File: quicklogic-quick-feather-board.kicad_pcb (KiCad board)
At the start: 6 copper layers, 50.8 x 22.9 mm, 88 parts, among them IC1 EOS-S3, J1 825437-4, J2 1x12_pinhead, J3 1x16_pinhead, J4 S2B-PH-SM4-TB_LF__SN_, J5 0473460001, J6 FTSH-105-01-L-DV-K, Q1 BSS138AKA, Q2 BSS84, Q3 RV1C002UN, Q4 RV1C002UN, Q5 RV1C002UN, U1 TPS62821DLCR, U2 MCP73831T-2ACI_OT, U3 GD25Q16CWIGR, U4 DPS310, U5 MC3635, X1 ECS-_327-12_5-34B-TR

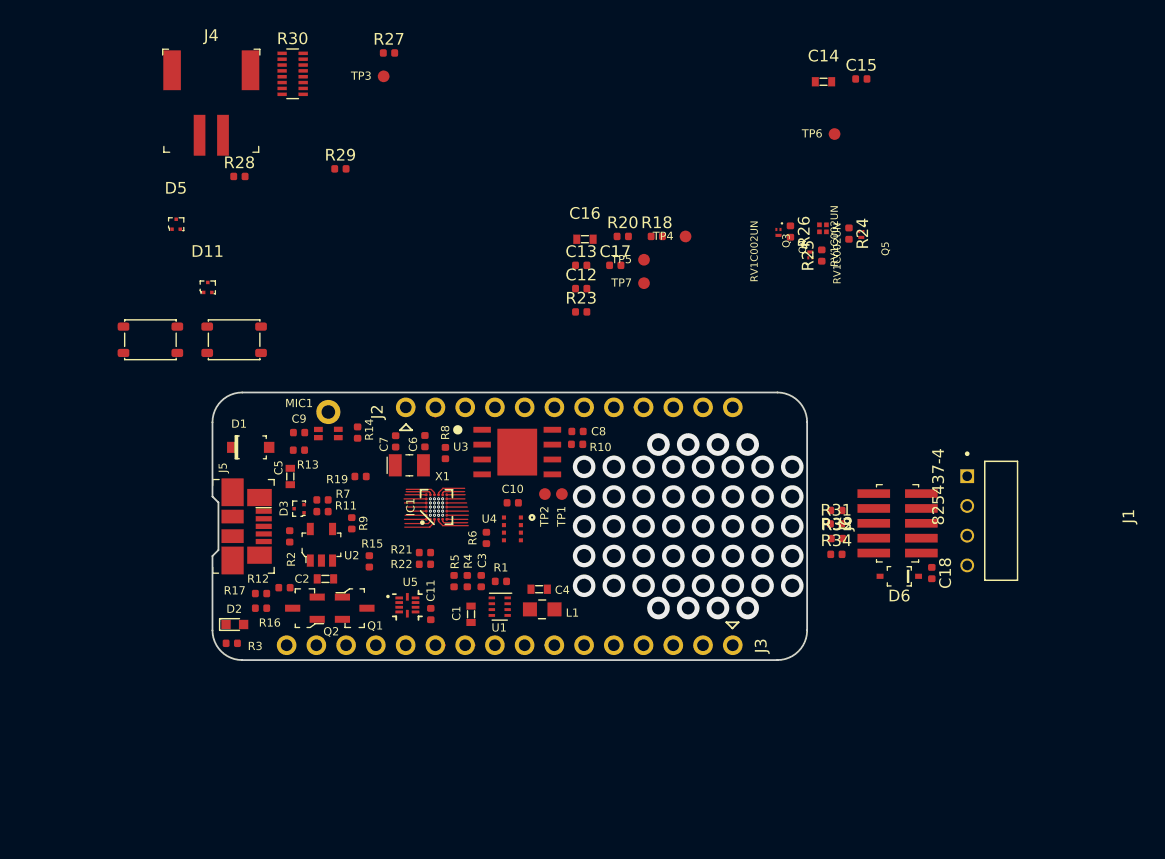
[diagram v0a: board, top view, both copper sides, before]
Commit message: Updated 3D models
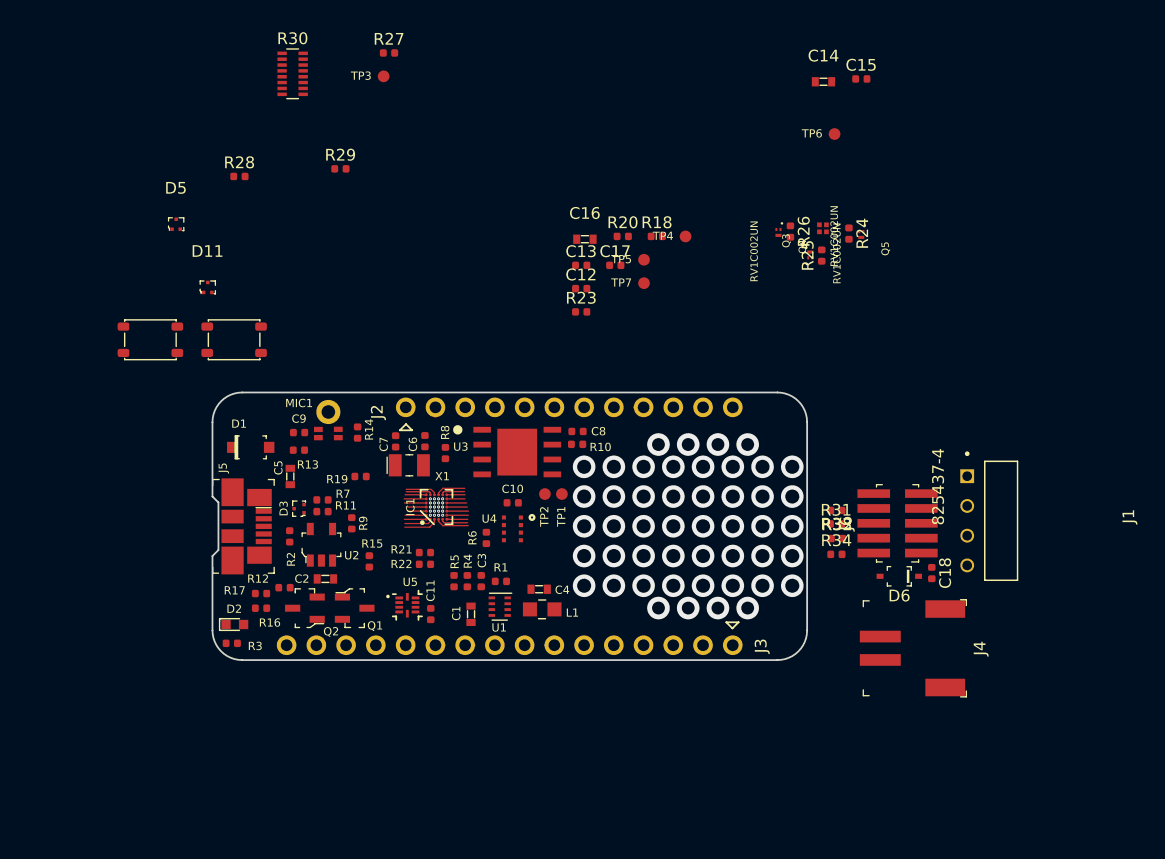
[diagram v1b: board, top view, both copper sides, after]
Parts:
- moved J4 72.0 mm to (180.2, 115.4), turned to 270 degrees

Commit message: Removed prototyping area, updated component placement
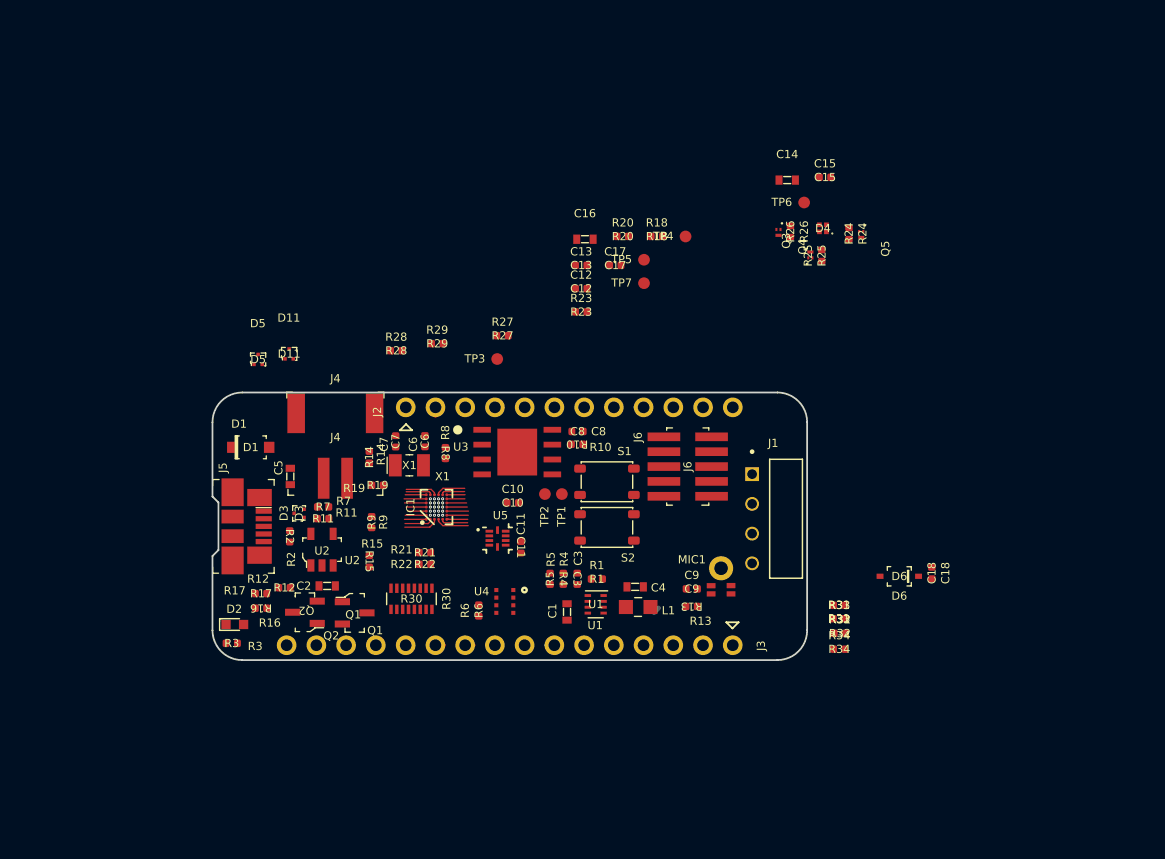
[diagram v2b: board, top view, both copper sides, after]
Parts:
- moved J4 48.8 mm to (133.6, 100.9), turned to 0 degrees
- moved R30 46.0 mm to (140.1, 111.2), turned to 270 degrees
- moved S1 40.8 mm to (156.8, 101.2), turned to 180 degrees
- moved C9 36.1 mm to (164.1, 110.3)
- moved MIC1 36.1 mm to (166.6, 108.6)
- moved R13 36.1 mm to (164.0, 111.8)
- moved S2 35.7 mm to (156.8, 105.1), turned to 180 degrees
- moved TP3 26.0 mm to (147.4, 90.8)
- moved R27 26.0 mm to (147.9, 88.7)
- moved R28 20.0 mm to (138.8, 90.0)
- moved J6 18.6 mm to (163.7, 99.9)
- moved J1 18.4 mm to (169.2, 100.5)
- moved R29 17.1 mm to (142.3, 89.4)
- moved D5 13.5 mm to (127.0, 90.8)
- moved C11 9.58 mm to (149.4, 106.8)
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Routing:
- net (no net): vias 48 -> 0
- removed copper zone on In2.Cu, net GND

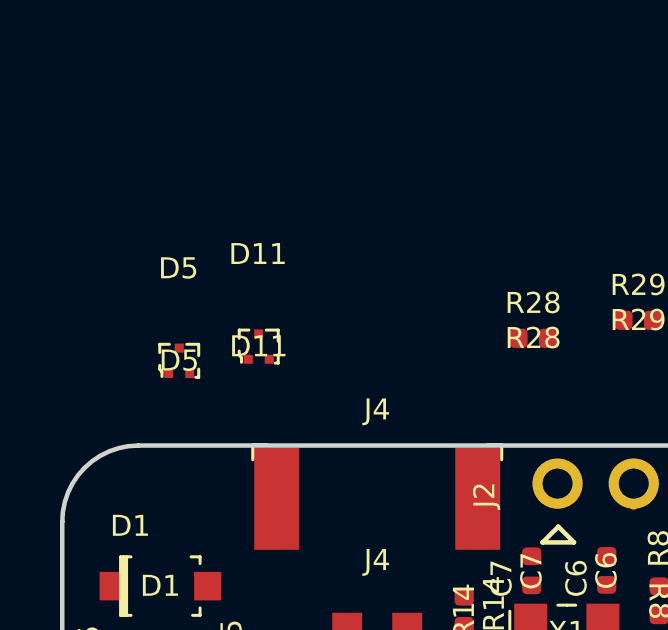
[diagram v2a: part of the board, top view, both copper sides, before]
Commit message: Changed MPN for buttons, updated 3D models
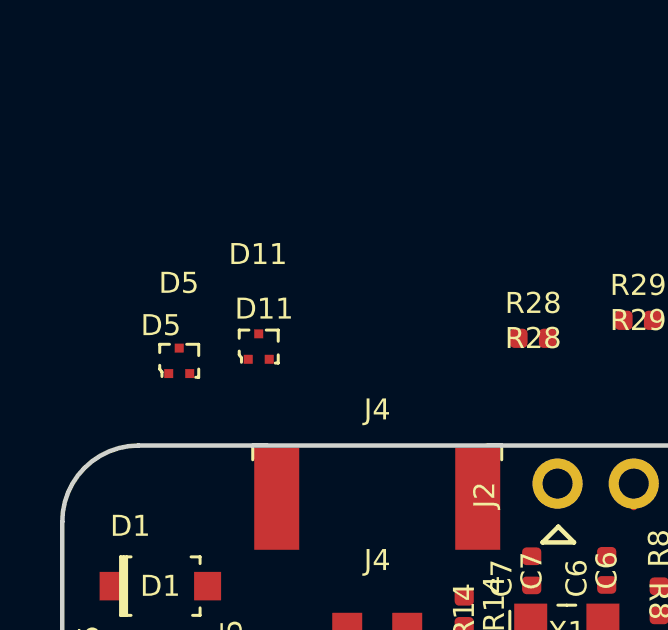
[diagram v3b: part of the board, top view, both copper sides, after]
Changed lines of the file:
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@@
-(kicad_pcb (version 20171130) (host pcbnew 5.1.4+dfsg1-1~bpo9+1)
+(kicad_pcb (version 20171130) (host pcbnew 5.1.4-e60b266~84~ubuntu18.04.1)
   (general
     (thickness 1.6)
@@
     (fp_line (start -0.525 0.225) (end -0.525 -0.425) (layer F.Fab) (width 0.1))
     (fp_line (start -0.35 0.425) (end 0.525 0.425) (layer F.Fab) (width 0.1))
-    (fp_text user %R (at 0 0) (layer F.SilkS)
+    (fp_text user %R (at 0.18 -1.255) (layer F.SilkS)
       (effects (font (size 0.7 0.7) (thickness 0.15)))
     )
@@
     (descr http://www.ti.com/lit/ds/symlink/tpd2eusb30.pdf)
     (attr smd)
-    (fp_text reference D5 (at -0.025 -3.075) (layer F.SilkS)
+    (fp_text reference D5 (at -0.01 -2.59) (layer F.SilkS)
       (effects (font (size 0.7 0.7) (thickness 0.15)))
     )
@@
     (fp_line (start -0.525 0.225) (end -0.525 -0.425) (layer F.Fab) (width 0.1))
     (fp_line (start -0.35 0.425) (end 0.525 0.425) (layer F.Fab) (width 0.1))
-    (fp_text user %R (at 0 0) (layer F.SilkS)
-      (effects (font (size 0.7 0.7) (thickness 0.15)))
-    )
+    (fp_text user %R (at -0.61 -1.18) (layer F.SilkS)
+      (effects (font (size 0.7 0.7) (thickness 0.15)))
+    )

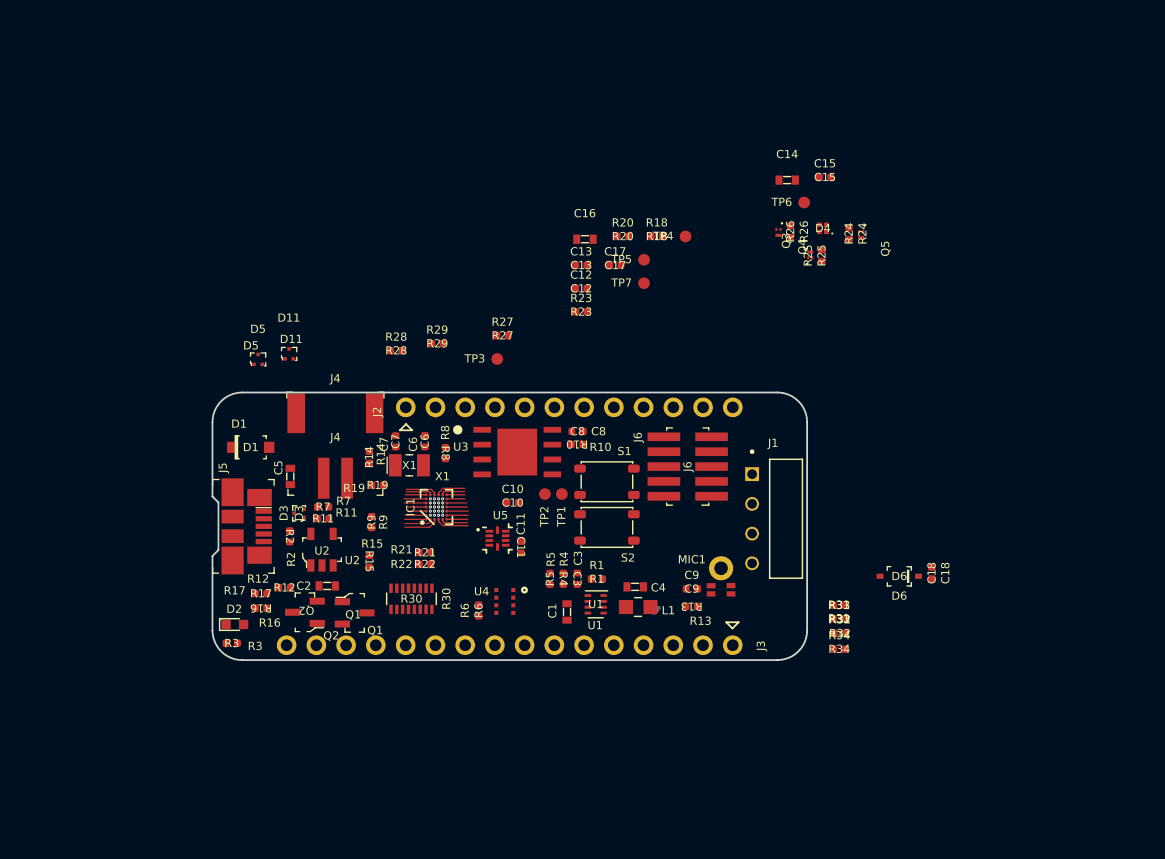
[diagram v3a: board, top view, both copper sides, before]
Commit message: Rearranged component placement
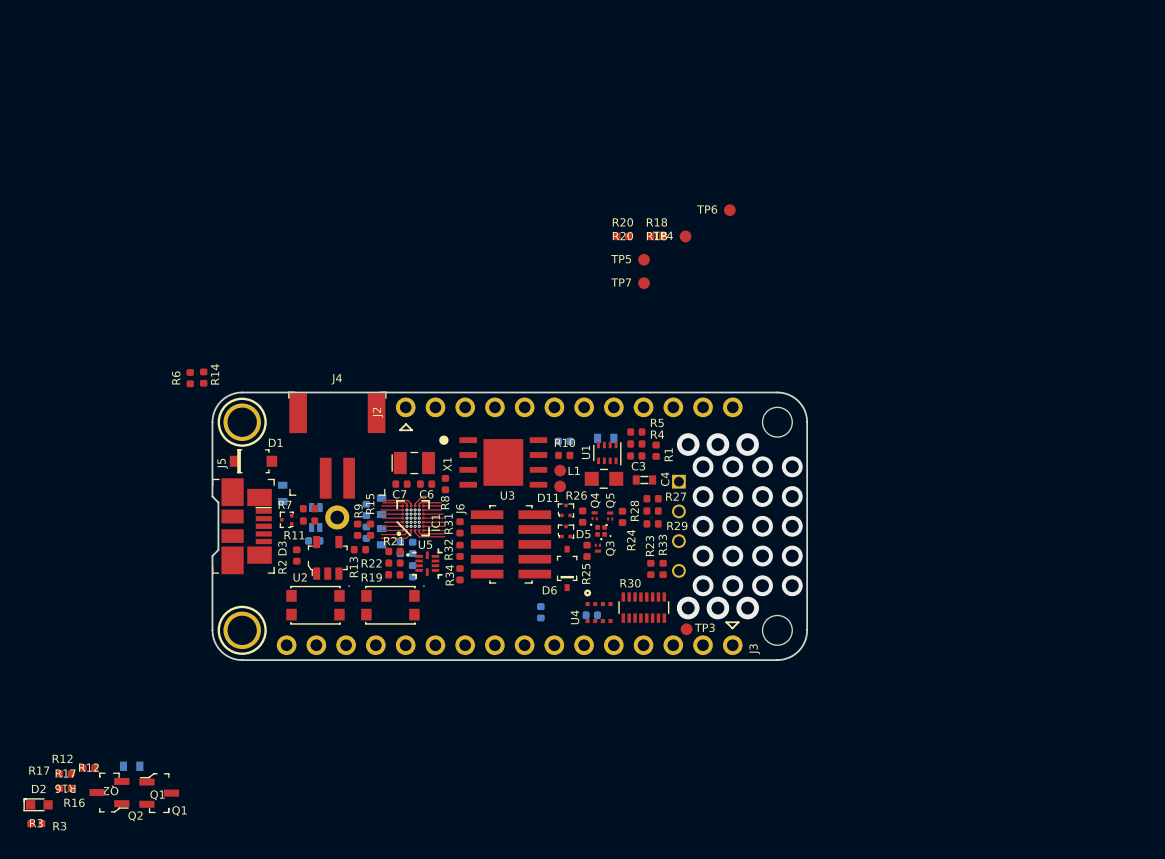
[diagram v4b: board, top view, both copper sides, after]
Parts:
- added @HOLE0: , , F.Cu at (171.8, 113.7)
- added @HOLE0: , , F.Cu at (171.6, 95.6)
- added U$31: MOUNTINGHOLE2.5, MOUNTINGHOLE_2.5_PLATED, F.Cu at (125.6, 96.1)
- added U$32: MOUNTINGHOLE2.5, MOUNTINGHOLE_2.5_PLATED, F.Cu at (125.6, 113.9)
- C1, C10, C11, C12, C13, C14, C15, C16, C17, C18, C2, C5, C8, C9, J1, MIC1: moved to B.Cu
- S1, S2: value TL3365AF180QG -> KMR2; footprint quicklogic-quick-feather-board-footprints:SW_SPST_4.2x3.2 -> quicklogic-quick-feather-board-footprints:SW_SPST_4.2x2.8
- moved C15 48.4 mm to (136.2, 103.6), turned to 90 degrees
- moved C14 44.5 mm to (137.6, 103.3), turned to 90 degrees
- moved C18 33.6 mm to (151.2, 112.3)
- moved R31 33.3 mm to (144.2, 105.1), turned to 270 degrees
- moved R32 33.2 mm to (144.2, 107.1), turned to 270 degrees
- moved MIC1 33.1 mm to (133.8, 104.2), turned to 90 degrees
- moved R34 33.0 mm to (144.2, 109.1), turned to 90 degrees
- moved C9 32.5 mm to (131.8, 106.2)
- moved Q5 32.3 mm to (157.1, 104.2), turned to 90 degrees
- moved R25 32.2 mm to (155.1, 107.1), turned to 270 degrees
- moved D4 32.1 mm to (156.3, 105.4)
- moved R6 31.6 mm to (121.2, 92.3)
- moved C17 31.2 mm to (136.2, 105.5), turned to 270 degrees
- moved R24 31.0 mm to (158.1, 104.2), turned to 90 degrees
- moved Q3 30.8 mm to (156.0, 106.8), turned to 270 degrees
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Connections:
- J2 pad 1: Net-(J2-Pad1) -> +VBAT
- J2 pad 12: +VBAT -> Net-(J2-Pad12)
- J3 pad 1: /SYS_RST -> GND
- J3 pad 13: Net-(J3-Pad13) -> GND
- J3 pad 15: Net-(J3-Pad15) -> +3V3
- J3 pad 16: GND -> /SYS_RST
- J3 pad 2: +3V3 -> Net-(J3-Pad2)
- J3 pad 4: GND -> Net-(J3-Pad4)
- J4 pad 1: +VBAT -> GND
- J4 pad 2: GND -> +VBAT
- R27 pad 1: Net-(J2-Pad4) -> Net-(J2-Pad9)
- R28 pad 1: Net-(J2-Pad2) -> Net-(J2-Pad11)
- R29 pad 1: Net-(J2-Pad1) -> Net-(J2-Pad12)
- R30 pad 10: Net-(J3-Pad14) -> Net-(J3-Pad3)
- R30 pad 11: Net-(J3-Pad13) -> Net-(J3-Pad4)
- R30 pad 12: Net-(J3-Pad12) -> Net-(J3-Pad5)
- R30 pad 13: Net-(J3-Pad11) -> Net-(J3-Pad6)
- R30 pad 14: Net-(J3-Pad10) -> Net-(J3-Pad7)
- R30 pad 9: Net-(J3-Pad15) -> Net-(J3-Pad2)
- S1 pad 1: /USR_BUTTON -> /SYS_RST
- S1 pad 2: Net-(S1-Pad2) -> GND
- S1 pad 3: GND -> Net-(S1-Pad3)
- S1 pad 4: Net-(S1-Pad4) -> (no net)
- S2 pad 1: /SYS_RST -> /USR_BUTTON
- S2 pad 2: Net-(S2-Pad2) -> GND
- S2 pad 3: GND -> Net-(S2-Pad3)
- S2 pad 4: Net-(S2-Pad4) -> (no net)
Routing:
- net /IMU_INT: track 2.57 -> 1.52 mm
- net Net-(J2-Pad2): track 0.76 -> 0.00 mm
- net GND: track 0.54 -> 0.00 mm, vias 9 -> 12
- net +VBAT: vias 0 -> 1
- net +3V3: vias 4 -> 7
- net (no net): vias 0 -> 19

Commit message: Finished component placement
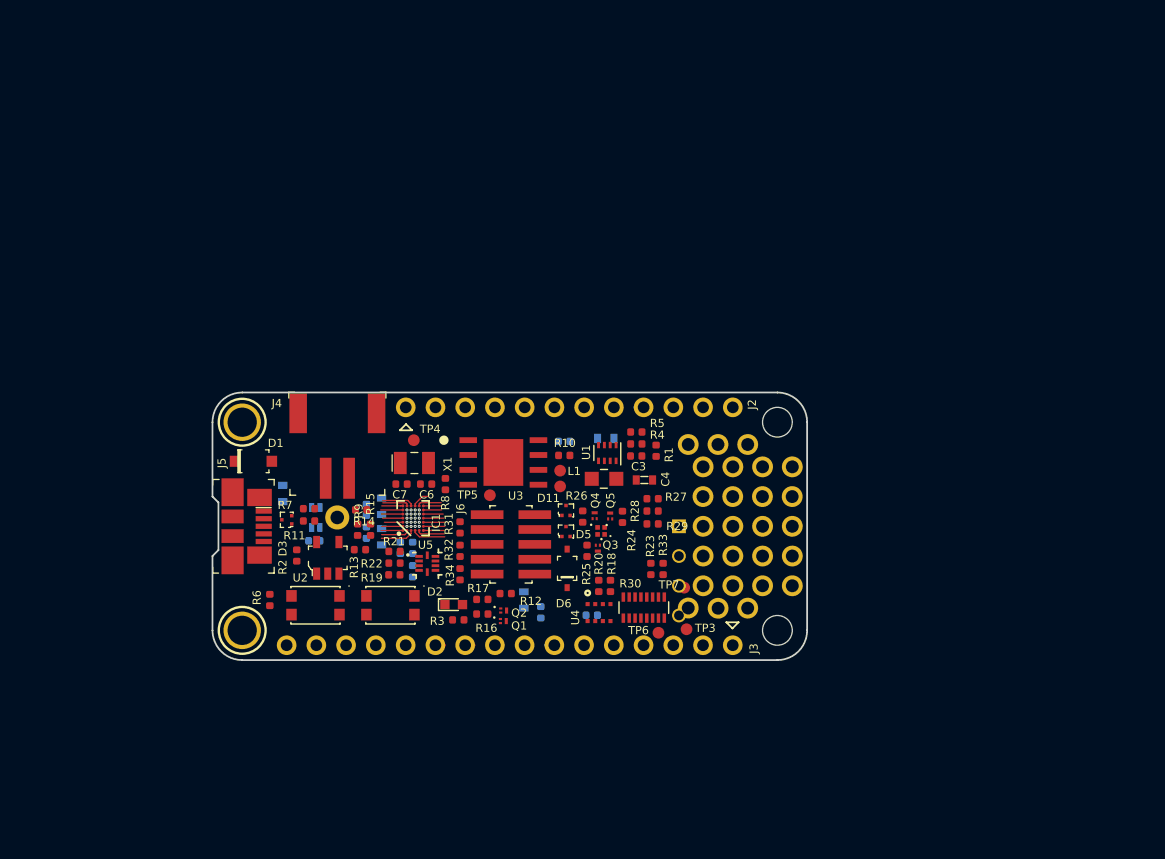
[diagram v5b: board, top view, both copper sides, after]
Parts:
- added REF**: PAD, quicklogic-quick-feather-board-footprints:PAD, F.Cu at (168.8, 112.0)
- added REF**: PAD, quicklogic-quick-feather-board-footprints:PAD, F.Cu at (167.5, 107.6)
- added REF**: PAD, quicklogic-quick-feather-board-footprints:PAD, F.Cu at (170.1, 107.6)
- added REF**: PAD, quicklogic-quick-feather-board-footprints:PAD, F.Cu at (172.6, 105.0)
- added REF**: PAD, quicklogic-quick-feather-board-footprints:PAD, F.Cu at (165.0, 105.0)
- added REF**: PAD, quicklogic-quick-feather-board-footprints:PAD, F.Cu at (167.5, 105.0)
- added REF**: PAD, quicklogic-quick-feather-board-footprints:PAD, F.Cu at (170.1, 105.0)
- added REF**: PAD, quicklogic-quick-feather-board-footprints:PAD, F.Cu at (172.6, 102.5)
- added REF**: PAD, quicklogic-quick-feather-board-footprints:PAD, F.Cu at (165.0, 102.5)
- added REF**: PAD, quicklogic-quick-feather-board-footprints:PAD, F.Cu at (167.5, 102.5)
- added REF**: PAD, quicklogic-quick-feather-board-footprints:PAD, F.Cu at (170.1, 102.5)
- added REF**: PAD, quicklogic-quick-feather-board-footprints:PAD, F.Cu at (166.3, 112.0)
- added REF**: PAD, quicklogic-quick-feather-board-footprints:PAD, F.Cu at (172.6, 100.0)
- added REF**: PAD, quicklogic-quick-feather-board-footprints:PAD, F.Cu at (170.1, 100.0)
- added REF**: PAD, quicklogic-quick-feather-board-footprints:PAD, F.Cu at (167.5, 100.0)
- added REF**: PAD, quicklogic-quick-feather-board-footprints:PAD, F.Cu at (165.0, 100.0)
- added REF**: PAD, quicklogic-quick-feather-board-footprints:PAD, F.Cu at (168.8, 98.0)
- added REF**: PAD, quicklogic-quick-feather-board-footprints:PAD, F.Cu at (166.3, 98.0)
- added REF**: PAD, quicklogic-quick-feather-board-footprints:PAD, F.Cu at (163.7, 98.0)
- added REF**: PAD, quicklogic-quick-feather-board-footprints:PAD, F.Cu at (163.7, 112.0)
- added REF**: PAD, quicklogic-quick-feather-board-footprints:PAD, F.Cu at (172.6, 110.1)
- added REF**: PAD, quicklogic-quick-feather-board-footprints:PAD, F.Cu at (165.0, 110.1)
- added REF**: PAD, quicklogic-quick-feather-board-footprints:PAD, F.Cu at (167.5, 110.1)
- added REF**: PAD, quicklogic-quick-feather-board-footprints:PAD, F.Cu at (170.1, 110.1)
- added REF**: PAD, quicklogic-quick-feather-board-footprints:PAD, F.Cu at (172.6, 107.6)
- added REF**: PAD, quicklogic-quick-feather-board-footprints:PAD, F.Cu at (165.0, 107.6)
- Q1: value BSS138AKA -> RV1C002UN; footprint quicklogic-quick-feather-board-footprints:SOT-23-3 -> quicklogic-quick-feather-board-footprints:VML0806
- Q2: value BSS84 -> RV1C001ZP; footprint quicklogic-quick-feather-board-footprints:SOT-23-3 -> quicklogic-quick-feather-board-footprints:VML0806
- moved R3 40.0 mm to (144.1, 113.0)
- moved D2 39.3 mm to (143.7, 111.7)
- moved R12 38.6 mm to (148.2, 110.8)
- moved R16 38.6 mm to (146.2, 112.5)
- moved R17 38.6 mm to (146.2, 111.2)
- moved Q2 37.0 mm to (147.9, 112.2), turned to 0 degrees
- moved TP6 36.6 mm to (161.2, 114.2)
- moved C2 36.4 mm to (149.7, 111.3), turned to 270 degrees
- moved Q1 32.8 mm to (147.9, 113.1)
- moved R18 30.1 mm to (157.1, 110.1), turned to 270 degrees
- moved R20 29.9 mm to (156.1, 110.1), turned to 270 degrees
- moved TP4 29.0 mm to (140.3, 97.7)
- moved TP7 26.2 mm to (163.4, 110.3)
- moved TP5 24.0 mm to (146.8, 102.4)
- moved R6 20.1 mm to (128.0, 111.3), turned to 270 degrees
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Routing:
- net GND: vias 12 -> 9
- net +VBAT: vias 1 -> 0
- net +3V3: vias 7 -> 4
- net (no net): vias 19 -> 0
